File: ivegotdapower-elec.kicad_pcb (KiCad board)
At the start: 2 copper layers, 100 x 50 mm, 0 parts

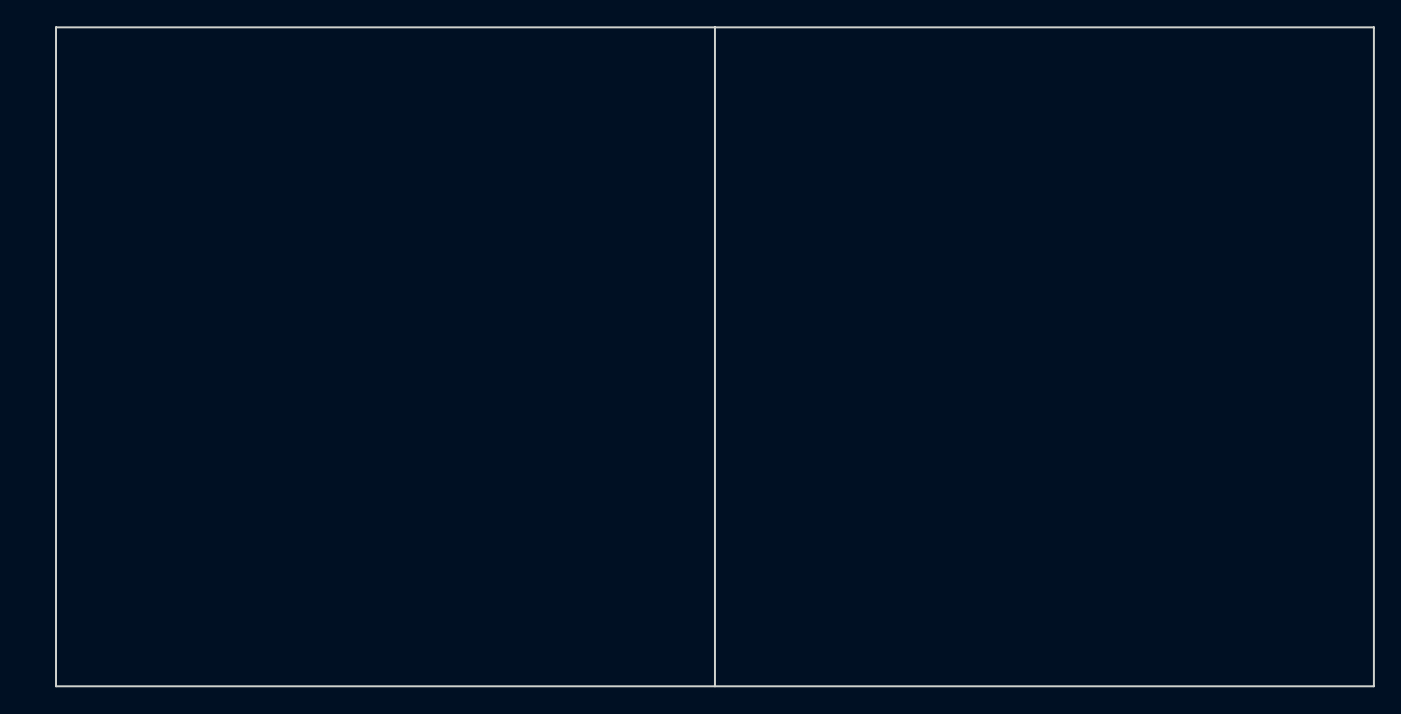
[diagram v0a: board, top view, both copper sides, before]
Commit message: Add most of interesting components.
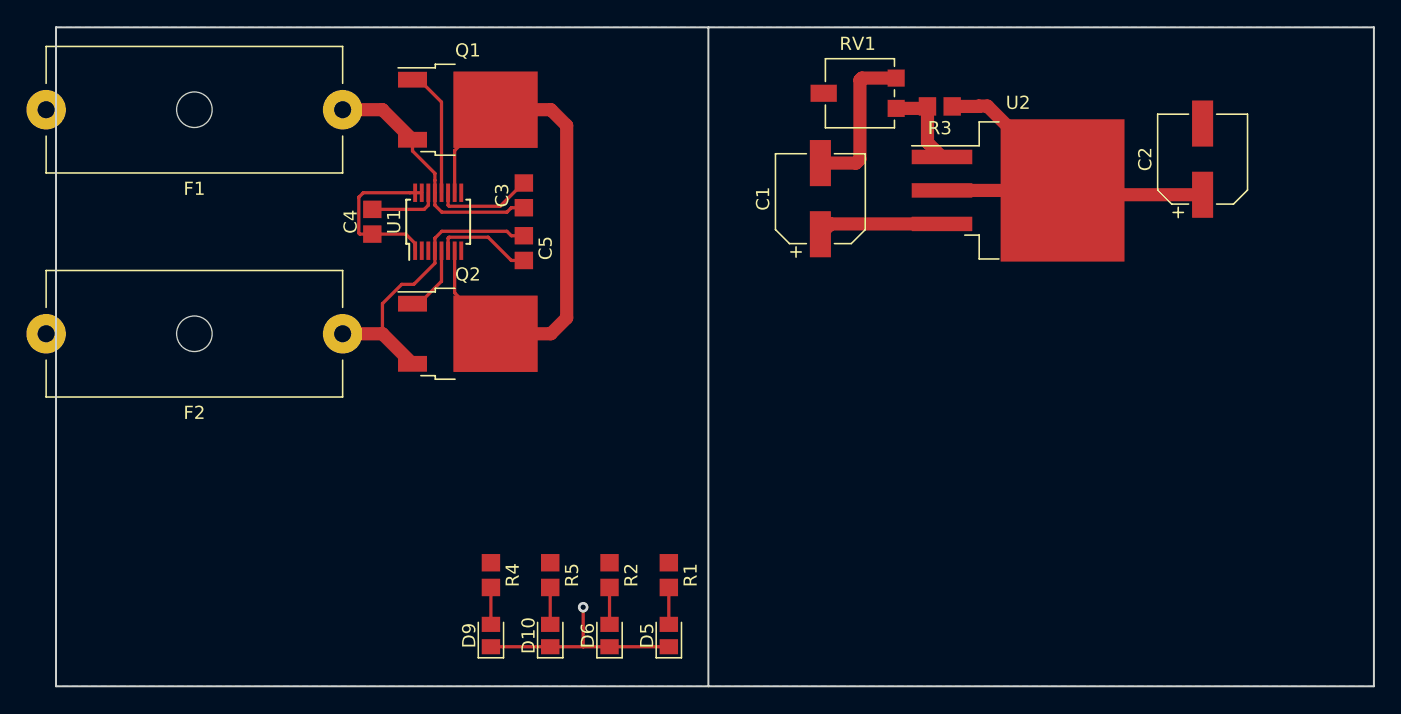
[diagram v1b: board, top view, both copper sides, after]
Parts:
- added C1: 10u, Capacitor_SMD:CP_Elec_6.3x5.8, F.Cu at (158.0, 113.0)
- added C2: 10u, Capacitor_SMD:CP_Elec_6.3x5.8, F.Cu at (187.0, 110.0)
- added C3: 56n, Capacitor_SMD:C_0805_2012Metric_Pad1.33x1.40mm_HandSolder, F.Cu at (135.5, 112.8)
- added C4: 100n, Capacitor_SMD:C_0805_2012Metric_Pad1.33x1.40mm_HandSolder, F.Cu at (124.0, 114.8)
- added C5: 56n, Capacitor_SMD:C_0805_2012Metric_Pad1.33x1.40mm_HandSolder, F.Cu at (135.5, 116.8)
- added D10: LED, LED_SMD:LED_0805_2012Metric_Pad1.15x1.40mm_HandSolder, F.Cu at (137.5, 146.2)
- added D5: LED, LED_SMD:LED_0805_2012Metric_Pad1.15x1.40mm_HandSolder, F.Cu at (146.5, 146.2)
- added D6: LED, LED_SMD:LED_0805_2012Metric_Pad1.15x1.40mm_HandSolder, F.Cu at (142.0, 146.2)
- added D9: LED, LED_SMD:LED_0805_2012Metric_Pad1.15x1.40mm_HandSolder, F.Cu at (133.0, 146.2)
- added F1: Fuse, Fuse:Fuseholder_Cylinder-5x20mm_Schurter_0031_8201_Horizontal_Open, F.Cu at (121.8, 106.2)
- added F2: Fuse, Fuse:Fuseholder_Cylinder-5x20mm_Schurter_0031_8201_Horizontal_Open, F.Cu at (121.8, 123.2)
- added Q1: IRF3205, Package_TO_SOT_SMD:TO-252-2, F.Cu at (131.2, 106.2)
- added Q2: IRF3205, Package_TO_SOT_SMD:TO-252-2, F.Cu at (131.2, 123.2)
- added R1: R, Resistor_SMD:R_0805_2012Metric_Pad1.33x1.40mm_HandSolder, F.Cu at (146.5, 141.6)
- added R2: R, Resistor_SMD:R_0805_2012Metric_Pad1.33x1.40mm_HandSolder, F.Cu at (142.0, 141.6)
- added R3: 120, Resistor_SMD:R_0805_2012Metric_Pad1.33x1.40mm_HandSolder, F.Cu at (167.1, 106.0)
- added R4: R, Resistor_SMD:R_0805_2012Metric_Pad1.33x1.40mm_HandSolder, F.Cu at (133.0, 141.6)
- added R5: R, Resistor_SMD:R_0805_2012Metric_Pad1.33x1.40mm_HandSolder, F.Cu at (137.5, 141.6)
- added RV1: R_POT, Potentiometer_SMD:Potentiometer_Vishay_TS53YL_Vertical, F.Cu at (161.0, 105.0)
- added U1: LTC4353, Package_SO:MSOP-16_3x4mm_P0.5mm, F.Cu at (129.0, 114.8)
- added U2: LM1084-ADJ, Package_TO_SOT_SMD:TO-263-3_TabPin2, F.Cu at (173.0, 112.4)
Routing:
- net /PowerInput: track 0.00 -> 41.6 mm
- net GND: track 0.00 -> 41.2 mm, vias 0 -> 1
- net /Out_Elec: track 0.00 -> 31.4 mm
- net /PowerInput_2: track 0.00 -> 22.8 mm
- net /PowerInput_1: track 0.00 -> 19.0 mm
- net Net-(Q1-Pad1): track 0.00 -> 9.78 mm
- net /In_Elec: track 0.00 -> 9.55 mm
- net Net-(C5-Pad2): track 0.00 -> 7.46 mm
- net Net-(C3-Pad2): track 0.00 -> 7.46 mm
- net Net-(R3-Pad2): track 0.00 -> 6.73 mm
- net Net-(C4-Pad2): track 0.00 -> 5.33 mm
- net Net-(Q2-Pad1): track 0.00 -> 5.22 mm
- net Net-(D9-Pad2): track 0.00 -> 2.80 mm
- net Net-(D6-Pad2): track 0.00 -> 2.80 mm
- net Net-(D5-Pad2): track 0.00 -> 2.80 mm
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- added copper zone on B.Cu, net GND
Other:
- outline, holes or cut-outs redrawn
- net class Power added: clearance 0.5, trace_width 1, via_dia 0.8, via_drill 0.4

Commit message: Add connectors, power footprints. Not sure of all footprints.
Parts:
- added CAN_R1: 120, Resistor_SMD:R_0805_2012Metric_Pad1.29x1.40mm_HandSolder, F.Cu at (182.9, 143.8)
- added D7: D_TVS, Diode_SMD:D_SMC_Handsoldering, F.Cu at (129.3, 107.8)
- added D8: D_TVS, Diode_SMD:D_SMC_Handsoldering, F.Cu at (129.3, 122.3)
- added J1: In1_Conn, Connector_Phoenix_MSTB:PhoenixContact_MSTBA_2,5_2-G_1x02_P5.00mm_Horizontal, F.Cu at (110.6, 106.3)
- added J2: In2_Conn, Connector_Phoenix_MSTB:PhoenixContact_MSTBA_2,5_2-G_1x02_P5.00mm_Horizontal, F.Cu at (110.6, 119.3)
- added J3: Conn_Power, Connector_Phoenix_MSTB:PhoenixContact_MSTBA_2,5_2-G_1x02_P5.00mm_Horizontal, F.Cu at (189.2, 129.0)
- added JP1: Jumper_NC_Small, Connector_PinHeader_2.54mm:PinHeader_1x02_P2.54mm_Vertical, F.Cu at (182.9, 140.4)
- added P1: CAN_conn, Connector_JST:JST_XH_B04B-XH-A_1x04_P2.50mm_Vertical, F.Cu at (197.0, 139.0)
- added P2: CAN_conn, Connector_JST:JST_XH_B04B-XH-A_1x04_P2.50mm_Vertical, F.Cu at (188.8, 139.0)
- added Q3: Q_NMOS_GDS, Package_TO_SOT_SMD:TO-252-2, F.Cu at (119.6, 106.5)
- added Q4: Q_NMOS_GDS, Package_TO_SOT_SMD:TO-252-2, F.Cu at (119.6, 119.5)
- F1, F2: footprint Fuse:Fuseholder_Cylinder-5x20mm_Schurter_0031_8201_Horizontal_Open -> Fuse:Fuse_1206_3216Metric_Pad1.39x1.80mm_HandSolder
- moved D6 60.4 mm to (195.8, 118.7), turned to 180 degrees
- moved R2 54.2 mm to (191.2, 118.7), turned to 0 degrees
- moved D5 50.5 mm to (195.8, 134.9), turned to 180 degrees
- moved R1 45.2 mm to (191.2, 134.9), turned to 0 degrees
- moved D9 39.1 mm to (134.8, 107.0), turned to 0 degrees
- moved R4 35.0 mm to (138.8, 107.0), turned to 180 degrees
- moved D10 25.3 mm to (134.8, 121.0), turned to 0 degrees
- moved R5 20.6 mm to (138.8, 121.0), turned to 180 degrees
- moved C3 18.5 mm to (154.0, 113.0)
- moved C4 18.5 mm to (142.5, 115.0)
- moved C5 18.5 mm to (154.0, 117.0)
- moved Q1 18.5 mm to (149.8, 106.5)
- moved Q2 18.5 mm to (149.8, 123.5)
- moved U1 18.5 mm to (147.5, 115.0)
- moved C1 6.71 mm to (164.6, 111.8)
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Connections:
- C1 pad 1: /In_Elec -> /Out_High
- Q1 pad 2: /PowerInput -> /Out_High
- Q2 pad 2: /PowerInput -> /Out_High
- U1 pad 10: /PowerInput -> /Out_High
- U1 pad 7: /PowerInput -> /Out_High
- U2 pad 3: /In_Elec -> /Out_High
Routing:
- net GND: track 41.2 -> 116.9 mm, vias 1 -> 0
- net /Out_High: track 0.00 -> 56.8 mm
- net /PowerInput: track 41.6 -> 0.00 mm
- net Net-(F2-Pad2): track 0.00 -> 26.9 mm
- net Net-(F1-Pad2): track 0.00 -> 26.9 mm
- net /Out_Elec: track 31.4 -> 55.5 mm, vias 0 -> 1
- net /PowerInput_2: track 22.8 -> 42.2 mm
- net /PowerInput_1: track 19.0 -> 35.6 mm
- net Net-(JP1-Pad2): track 0.00 -> 16.3 mm
- net /In1_Status: track 0.00 -> 13.4 mm, vias 0 -> 2
- net Net-(CAN_R1-Pad1): track 0.00 -> 13.2 mm
- net /In2_Status: track 0.00 -> 12.9 mm, vias 0 -> 2
- net /In_Elec: track 9.55 -> 0.00 mm
- net Net-(J1-Pad1): track 0.00 -> 5.88 mm
- net Net-(J2-Pad1): track 0.00 -> 5.86 mm
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- added copper zone on F.Cu, net GND
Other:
- outline, holes or cut-outs redrawn

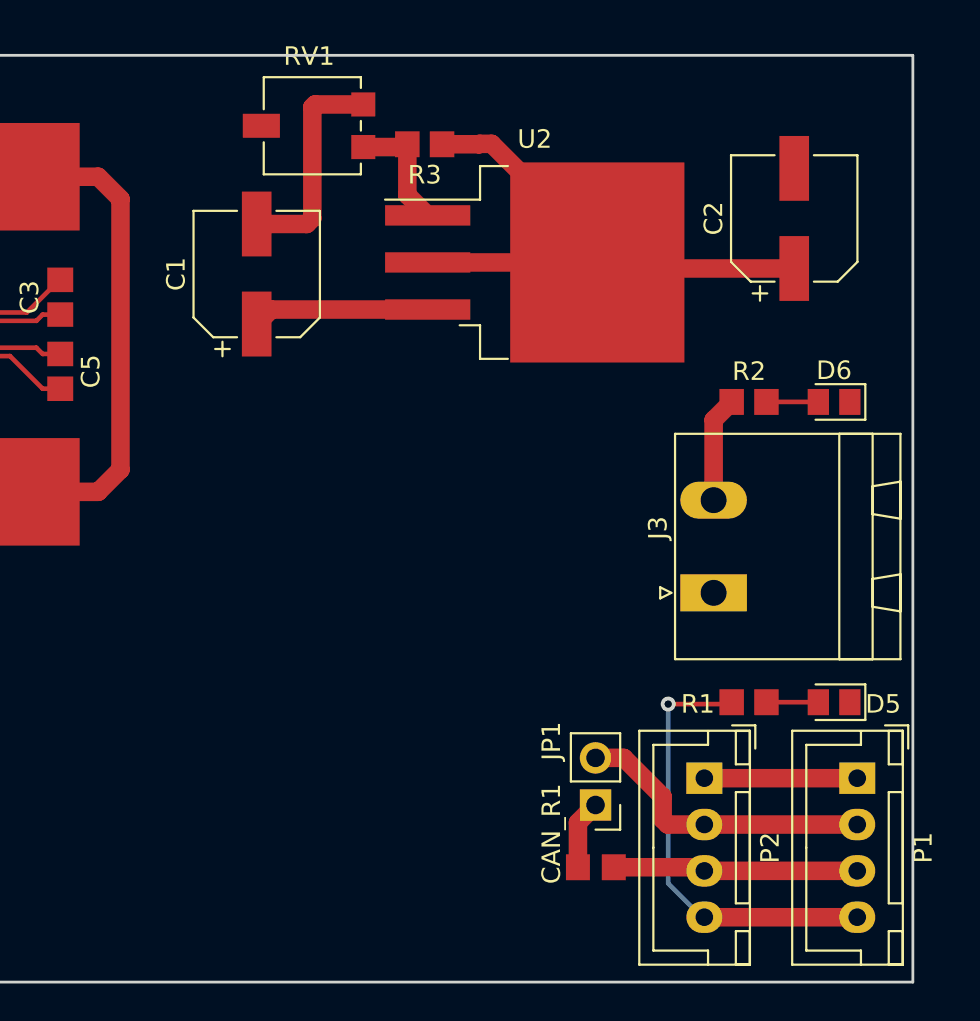
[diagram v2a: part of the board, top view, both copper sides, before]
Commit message: Small reorganization. There is space left for stm32.
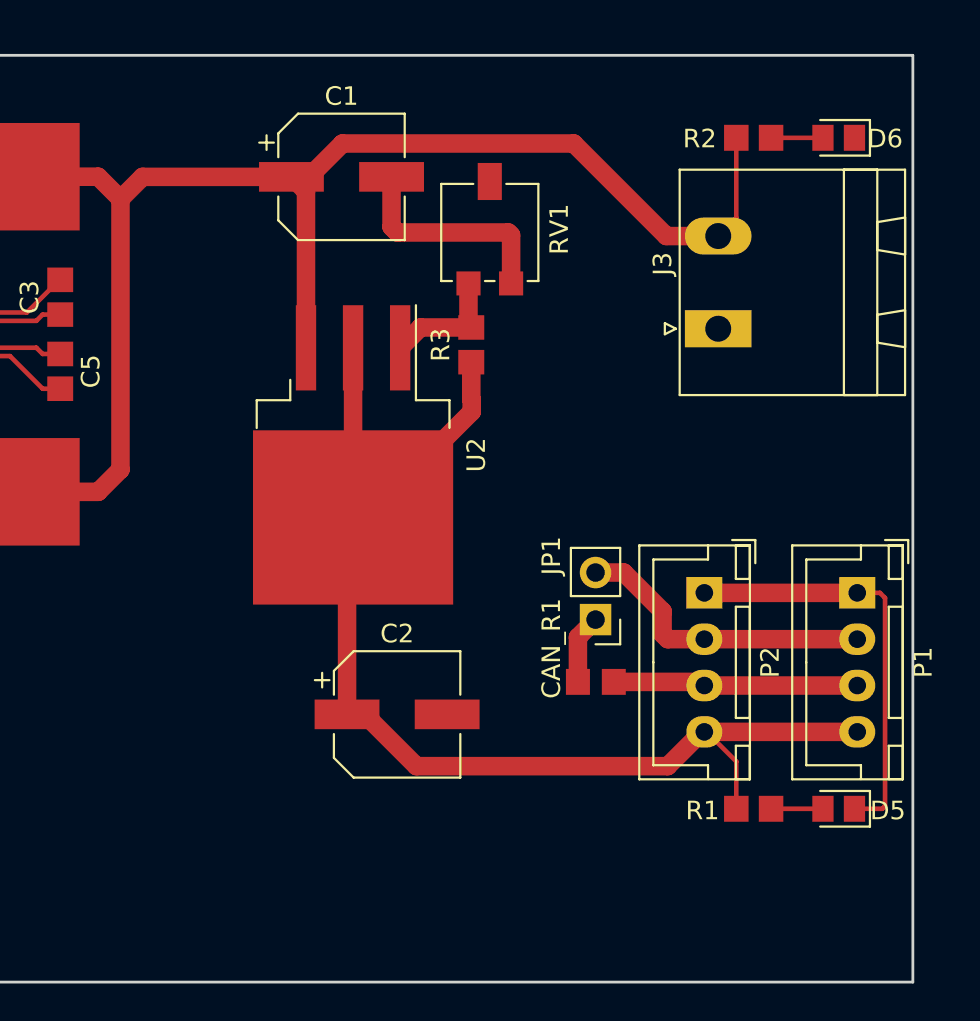
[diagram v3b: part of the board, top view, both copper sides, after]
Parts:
- moved C2 34.3 mm to (172.2, 135.6), turned to 0 degrees
- moved U2 14.3 mm to (169.8, 121.6), turned to 270 degrees
- moved D6 14.3 mm to (196.0, 104.5)
- moved J3 14.3 mm to (189.5, 114.8)
- moved R2 14.3 mm to (191.4, 104.5)
- moved RV1 11.2 mm to (177.2, 109.6), turned to 270 degrees
- moved R3 11.1 mm to (176.2, 115.6), turned to 90 degrees
- moved CAN_R1 10.0 mm to (182.9, 133.8)
- moved JP1 10.0 mm to (182.9, 130.4)
- moved P1 10.0 mm to (197.0, 129.0)
- moved P2 10.0 mm to (188.8, 129.0)
- moved C1 6.96 mm to (169.2, 106.6), turned to 0 degrees
- moved D5 5.76 mm to (196.0, 140.7)
- moved R1 5.76 mm to (191.4, 140.7)
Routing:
- net /Out_High: track 56.8 -> 92.4 mm
- net GND: track 116.9 -> 131.4 mm
- net /Out_Elec: track 55.5 -> 65.7 mm, vias 1 -> 0

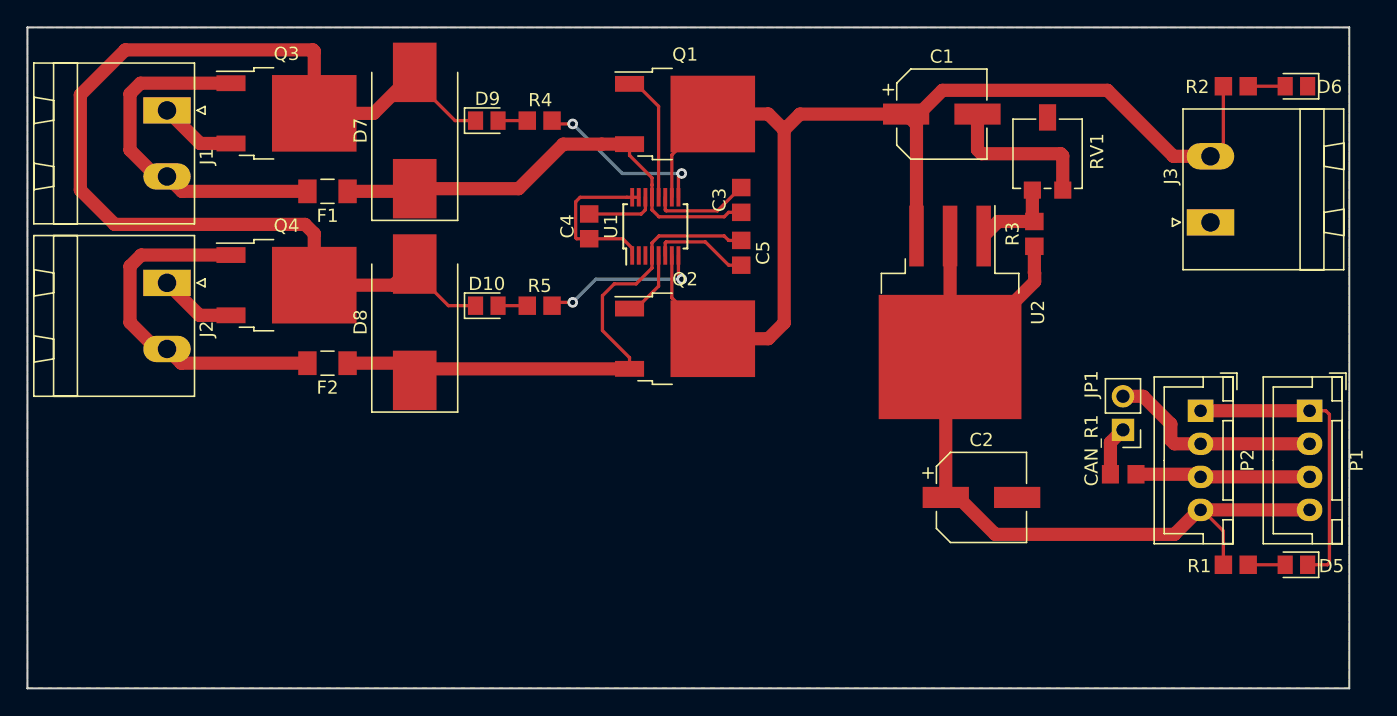
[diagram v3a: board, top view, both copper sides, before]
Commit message: Set footprints, cleanup PCB of old componnents
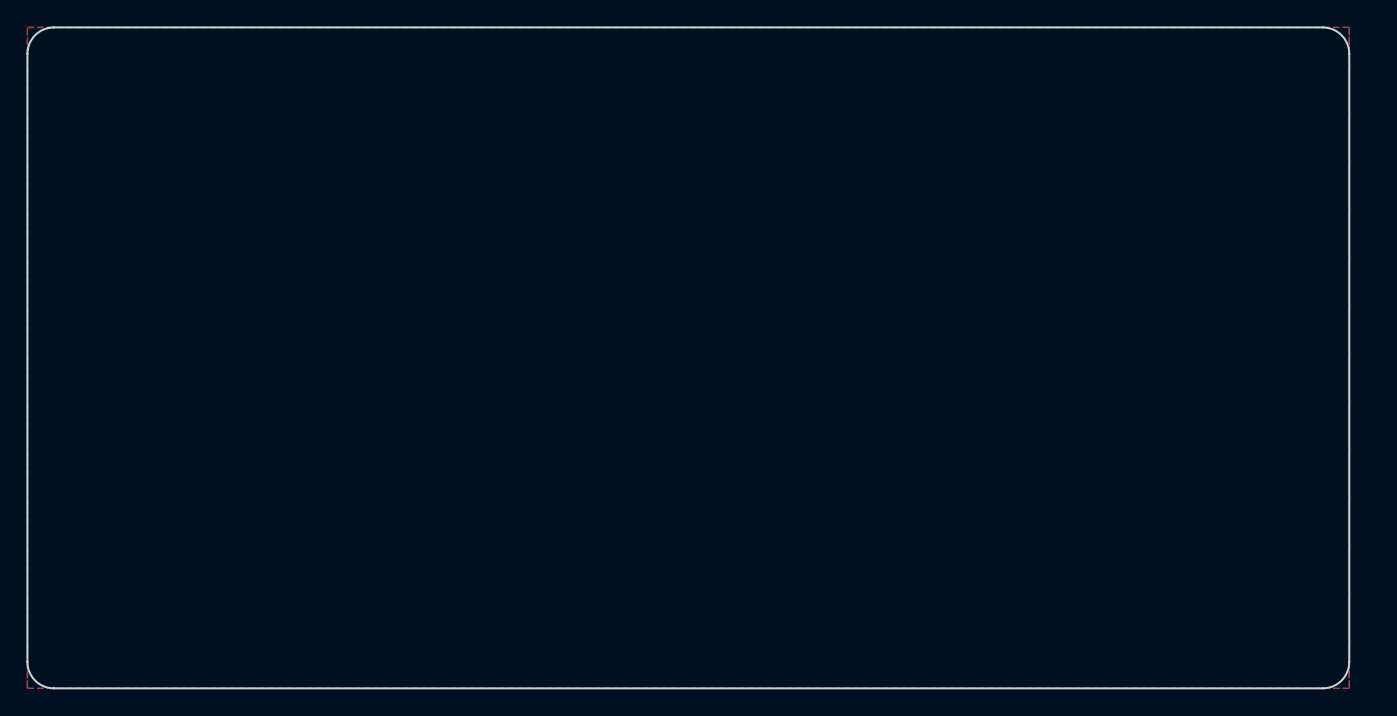
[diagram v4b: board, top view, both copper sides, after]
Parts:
- removed C1, C2: 10u, Capacitor_SMD:CP_Elec_6.3x5.8
- removed C3, C5: 56n, Capacitor_SMD:C_0805_2012Metric_Pad1.33x1.40mm_HandSolder
- removed C4: 100n, Capacitor_SMD:C_0805_2012Metric_Pad1.33x1.40mm_HandSolder
- removed CAN_R1: 120, Resistor_SMD:R_0805_2012Metric_Pad1.29x1.40mm_HandSolder
- removed D10, D5, D6, D9: LED, LED_SMD:LED_0805_2012Metric_Pad1.15x1.40mm_HandSolder
- removed D7, D8: D_TVS, Diode_SMD:D_SMC_Handsoldering
- removed F1, F2: Fuse, Fuse:Fuse_1206_3216Metric_Pad1.39x1.80mm_HandSolder
- removed J1: In1_Conn, Connector_Phoenix_MSTB:PhoenixContact_MSTBA_2,5_2-G_1x02_P5.00mm_Horizontal
- removed J2: In2_Conn, Connector_Phoenix_MSTB:PhoenixContact_MSTBA_2,5_2-G_1x02_P5.00mm_Horizontal
- removed J3: Conn_Power, Connector_Phoenix_MSTB:PhoenixContact_MSTBA_2,5_2-G_1x02_P5.00mm_Horizontal
- removed JP1: Jumper_NC_Small, Connector_PinHeader_2.54mm:PinHeader_1x02_P2.54mm_Vertical
- removed P1, P2: CAN_conn, Connector_JST:JST_XH_B04B-XH-A_1x04_P2.50mm_Vertical
- removed Q1, Q2: IRF3205, Package_TO_SOT_SMD:TO-252-2
- removed Q3, Q4: Q_NMOS_GDS, Package_TO_SOT_SMD:TO-252-2
- removed R1, R2, R4, R5: R, Resistor_SMD:R_0805_2012Metric_Pad1.33x1.40mm_HandSolder
- removed R3: 120, Resistor_SMD:R_0805_2012Metric_Pad1.33x1.40mm_HandSolder
- removed RV1: R_POT, Potentiometer_SMD:Potentiometer_Vishay_TS53YL_Vertical
- removed U1: LTC4353, Package_SO:MSOP-16_3x4mm_P0.5mm
- removed U2: LM1084-ADJ, Package_TO_SOT_SMD:TO-263-3_TabPin2
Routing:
- net GND: track 131.4 -> 0.00 mm
- net /Out_High: track 92.4 -> 0.00 mm
- net /Out_Elec: track 65.7 -> 0.00 mm
- net /PowerInput_2: track 42.2 -> 0.00 mm
- net /PowerInput_1: track 35.6 -> 0.00 mm
- net Net-(F2-Pad2): track 26.9 -> 0.00 mm
- net Net-(F1-Pad2): track 26.9 -> 0.00 mm
- net Net-(JP1-Pad2): track 16.3 -> 0.00 mm
- net /In1_Status: track 13.4 -> 0.00 mm, vias 2 -> 0
- net Net-(CAN_R1-Pad1): track 13.2 -> 0.00 mm
- net /In2_Status: track 12.9 -> 0.00 mm, vias 2 -> 0
- net Net-(Q1-Pad1): track 9.78 -> 0.00 mm
- net Net-(C5-Pad2): track 7.46 -> 0.00 mm
- net Net-(C3-Pad2): track 7.46 -> 0.00 mm
- net Net-(R3-Pad2): track 6.73 -> 0.00 mm
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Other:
- outline, holes or cut-outs redrawn
